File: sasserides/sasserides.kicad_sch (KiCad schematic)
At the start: 132 parts, among them J1 Conn_02x16_Odd_Even, Q1 2N7002, U1 CDCV304PW

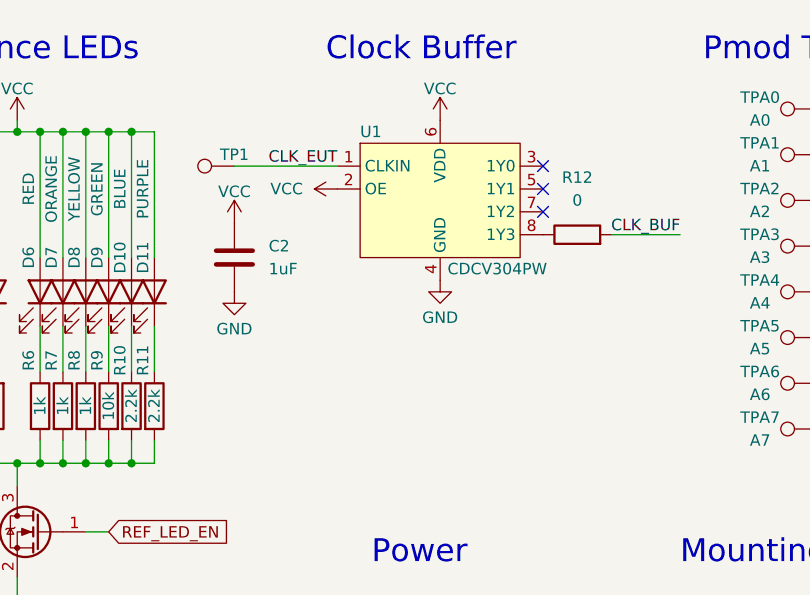
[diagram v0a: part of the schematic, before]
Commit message: Add a 1M pulldown resistor at clock buffer input.
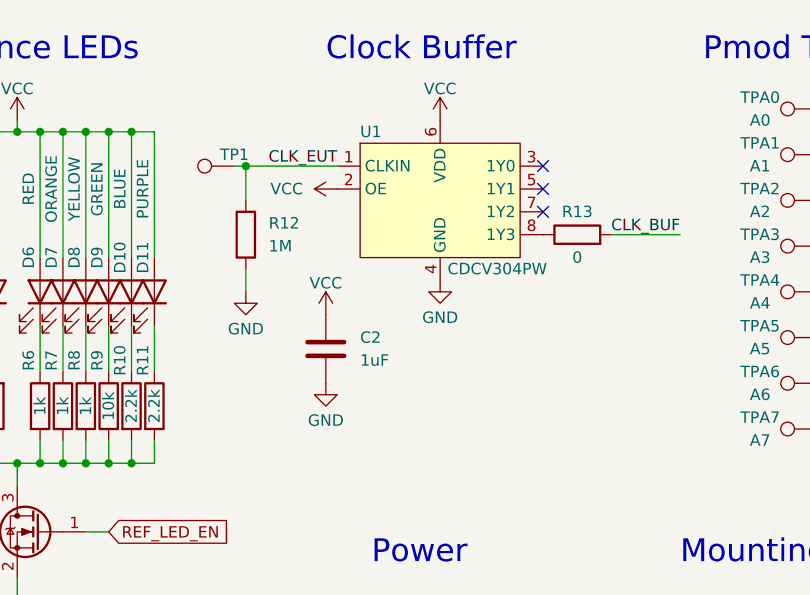
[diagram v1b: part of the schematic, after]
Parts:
- added R12: 1M, Resistor_SMD:R_0402_1005Metric, symbol Device:R
- renumbered R12 to R13
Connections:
- net CLK_EUT: now also R12.2
- net GND: now also R12.1
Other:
- moved on the sheet: C2
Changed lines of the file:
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@@
   (junction (at 33.02 114.3) (diameter 0) (color 0 0 0 0)
   )
+  (junction (at 60.96 118.11) (diameter 0) (color 0 0 0 0)
+  )
   (junction (at 45.72 114.3) (diameter 0) (color 0 0 0 0)
   )
@@
     (stroke (width 0) (type default))
   )
-  (wire (pts (xy 71.12 118.11) (xy 59.69 118.11))
+  (wire (pts (xy 71.12 118.11) (xy 60.96 118.11))
     (stroke (width 0) (type default))
   )
@@
     (stroke (width 0) (type default))
   )
+  (wire (pts (xy 60.96 118.11) (xy 60.96 121.92))
+    (stroke (width 0) (type default))
+  )
   (wire (pts (xy 85.09 74.93) (xy 106.68 74.93))
     (stroke (width 0) (type default))
@@
     (stroke (width 0) (type default))
   )
+  (wire (pts (xy 60.96 129.54) (xy 60.96 132.08))
+    (stroke (width 0) (type default))
+  )
   (wire (pts (xy 27.94 151.13) (xy 30.48 151.13))
     (stroke (width 0) (type default))
@@
     (stroke (width 0) (type default))
   )
+  (wire (pts (xy 60.96 118.11) (xy 59.69 118.11))
+    (stroke (width 0) (type default))
+  )
   (wire (pts (xy 25.4 128.27) (xy 25.4 114.3))
     (stroke (width 0) (type default))
@@
     )
   )
-  (symbol (lib_id "power:VCC") (at 59.69 124.46 0) (unit 1)
+  (symbol (lib_id "power:VCC") (at 69.85 134.62 0) (unit 1)
     (in_bom yes) (on_board yes) (dnp no)
-    (property "Reference" "#PWR011" (at 59.69 128.27 0)
+    (property "Reference" "#PWR011" (at 69.85 138.43 0)
       (effects (font (size 1.27 1.27)) hide)
     )
-    (property "Value" "VCC" (at 59.69 120.9581 0)
+    (property "Value" "VCC" (at 69.85 131.1181 0)
       (effects (font (size 1.27 1.27)))
     )
-    (property "Footprint" "" (at 59.69 124.46 0)
+    (property "Footprint" "" (at 69.85 134.62 0)
       (effects (font (size 1.27 1.27)) hide)
     )
-    (property "Datasheet" "" (at 59.69 124.46 0)
+    (property "Datasheet" "" (at 69.85 134.62 0)
       (effects (font (size 1.27 1.27)) hide)
     )
@@
     )
   )
-  (symbol (lib_id "Device:C") (at 59.69 128.27 0) (unit 1)
+  (symbol (lib_id "Device:C") (at 69.85 138.43 0) (unit 1)
     (in_bom yes) (on_board yes) (dnp no)
-    (property "Reference" "C2" (at 63.5 127 0)
+    (property "Reference" "C2" (at 73.66 137.16 0)
       (effects (font (size 1.27 1.27)) (justify left))
     )
-    (property "Value" "1uF" (at 63.5 129.54 0)
+    (property "Value" "1uF" (at 73.66 139.7 0)
       (effects (font (size 1.27 1.27)) (justify left))
     )
-    (property "Footprint" "Capacitor_SMD:C_0805_2012Metric" (at 60.6552 132.08 0)
+    (property "Footprint" "Capacitor_SMD:C_0805_2012Metric" (at 70.8152 142.24 0)
       (effects (font (size 1.27 1.27)) hide)
     )
-    (property "Datasheet" "~" (at 59.69 128.27 0)
+    (property "Datasheet" "~" (at 69.85 138.43 0)
       (effects (font (size 1.27 1.27)) hide)
     )
@@
     )
   )
-  (symbol (lib_id "power:GND") (at 59.69 132.08 0) (unit 1)
+  (symbol (lib_id "power:GND") (at 69.85 142.24 0) (unit 1)
     (in_bom yes) (on_board yes) (dnp no)
-    (property "Reference" "#PWR012" (at 59.69 138.43 0)
+    (property "Reference" "#PWR012" (at 69.85 148.59 0)
       (effects (font (size 1.27 1.27)) hide)
     )
-    (property "Value" "GND" (at 59.69 136.2155 0)
+    (property "Value" "GND" (at 69.85 146.3755 0)
       (effects (font (size 1.27 1.27)))
     )
-    (property "Footprint" "" (at 59.69 132.08 0)
+    (property "Footprint" "" (at 69.85 142.24 0)
       (effects (font (size 1.27 1.27)) hide)
     )
-    (property "Datasheet" "" (at 59.69 132.08 0)
+    (property "Datasheet" "" (at 69.85 142.24 0)
       (effects (font (size 1.27 1.27)) hide)
     )
@@
   )
   (symbol (lib_id "Device:R") (at 97.79 125.73 90) (unit 1)
-    (in_bom yes) (on_board yes) (dnp no) (fields_autoplaced)
-    (property "Reference" "R12" (at 97.79 119.38 90)
+    (in_bom yes) (on_board yes) (dnp no)
+    (property "Reference" "R13" (at 97.79 123.19 90)
       (effects (font (size 1.27 1.27)))
     )
-    (property "Value" "0" (at 97.79 121.92 90)
+    (property "Value" "0" (at 97.79 128.27 90)
       (effects (font (size 1.27 1.27)))
     )
@@
       (project "sasserides"
         (path "/29d14f83-224e-4982-8820-b9fb63f3a50c"
-          (reference "R12") (unit 1)
+          (reference "R13") (unit 1)
         )
       )
@@
     )
   )
+  (symbol (lib_id "power:GND") (at 60.96 132.08 0) (mirror y) (unit 1)
+    (in_bom yes) (on_board yes) (dnp no) (fields_autoplaced)
+    (property "Reference" "#PWR014" (at 60.96 138.43 0)
+      (effects (font (size 1.27 1.27)) hide)
+    )
+    (property "Value" "GND" (at 60.96 136.2155 0)
+      (effects (font (size 1.27 1.27)))
+    )
+    (property "Footprint" "" (at 60.96 132.08 0)
+      (effects (font (size 1.27 1.27)) hide)
+    )
+    (property "Datasheet" "" (at 60.96 132.08 0)
+      (effects (font (size 1.27 1.27)) hide)
+    )
+    (pin "1")
+    (instances
+      (project "sasserides"
+        (path "/29d14f83-224e-4982-8820-b9fb63f3a50c"
+          (reference "#PWR014") (unit 1)
+        )
+      )
+    )
+  )
   (symbol (lib_id "Device:C") (at 24.13 162.56 0) (mirror y) (unit 1)
     (in_bom yes) (on_board yes) (dnp no)
@@
         )
       )
+    )
+  )
+  (symbol (lib_id "Device:R") (at 60.96 125.73 180) (unit 1)
+    (in_bom yes) (on_board yes) (dnp no)
+    (property "Reference" "R12" (at 63.5 124.46 0)
+      (effects (font (size 1.27 1.27)) (justify right))
+    )
+    (property "Value" "1M" (at 63.5 127 0)
+      (effects (font (size 1.27 1.27)) (justify right))
+    )
+    (property "Footprint" "Resistor_SMD:R_0402_1005Metric" (at 62.738 125.73 90)
+      (effects (font (size 1.27 1.27)) hide)
+    )
+    (property "Datasheet" "~" (at 60.96 125.73 0)
+      (effects (font (size 1.27 1.27)) hide)
+    )
+    (pin "1")
+    (pin "2")
+    (instances
+      (project "sasserides"
+        (path "/29d14f83-224e-4982-8820-b9fb63f3a50c"
+          (reference "R12") (unit 1)
+        )
+      )

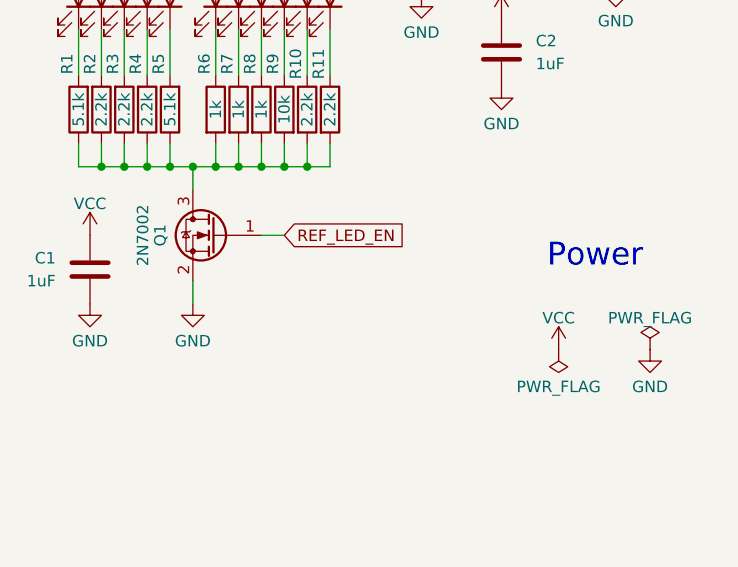
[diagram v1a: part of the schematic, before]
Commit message: Add 10k pulldown to Q1 gate.
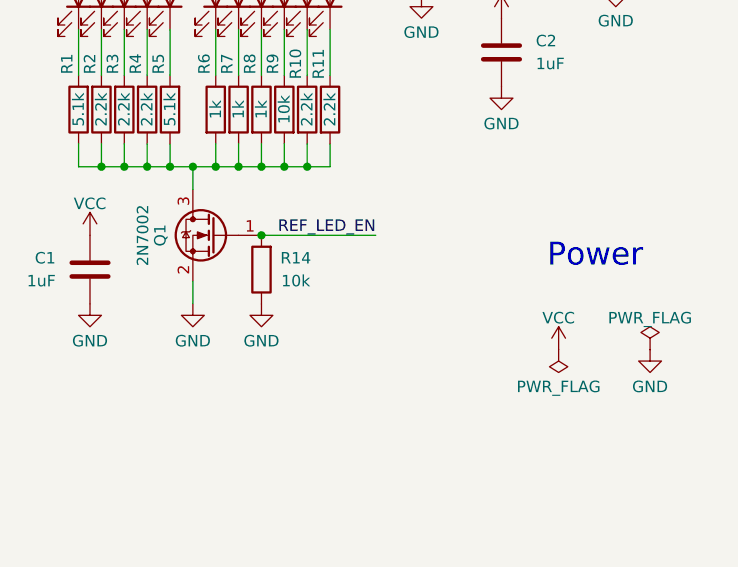
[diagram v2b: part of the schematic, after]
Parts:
- added R14: 10k, Resistor_SMD:R_0402_1005Metric, symbol Device:R
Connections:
- net GND: now also R14.1
- net REF_LED_EN: now also R14.2
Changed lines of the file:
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@@
   (junction (at 40.64 114.3) (diameter 0) (color 0 0 0 0)
   )
+  (junction (at 43.18 158.75) (diameter 0) (color 0 0 0 0)
+  )
   (junction (at 45.72 151.13) (diameter 0) (color 0 0 0 0)
   )
@@
     (stroke (width 0) (type default))
   )
-  (wire (pts (xy 45.72 158.75) (xy 43.18 158.75))
+  (wire (pts (xy 55.88 158.75) (xy 43.18 158.75))
     (stroke (width 0) (type default))
   )
@@
     (effects (font (size 2.54 2.54)) (justify left bottom))
   )
+  (label "REF_LED_EN" (at 55.88 158.75 180) (fields_autoplaced)
+    (effects (font (size 1.27 1.27)) (justify right bottom))
+  )
   (label "D2 3V3-Vf" (at 54.61 92.71 0) (fields_autoplaced)
     (effects (font (size 1.27 1.27)) (justify left bottom))
@@
     (effects (font (size 1.27 1.27)) (justify left bottom))
   )
-  (global_label "REF_LED_EN" (shape input) (at 45.72 158.75 0) (fields_autoplaced)
-    (effects (font (size 1.27 1.27)) (justify left))
-    (property "Intersheetrefs" "${INTERSHEET_REFS}" (at 59.9952 158.75 0)
-      (effects (font (size 1.27 1.27)) (justify left) hide)
-    )
-  )
   (symbol (lib_id "Connector:TestPoint") (at 203.2 59.69 90) (unit 1)
     (in_bom yes) (on_board yes) (dnp no)
@@
     )
   )
+  (symbol (lib_id "Device:R") (at 43.18 162.56 180) (unit 1)
+    (in_bom yes) (on_board yes) (dnp no)
+    (property "Reference" "R14" (at 46.99 161.29 0)
+      (effects (font (size 1.27 1.27)))
+    )
+    (property "Value" "10k" (at 46.99 163.83 0)
+      (effects (font (size 1.27 1.27)))
+    )
+    (property "Footprint" "Resistor_SMD:R_0402_1005Metric" (at 44.958 162.56 90)
+      (effects (font (size 1.27 1.27)) hide)
+    )
+    (property "Datasheet" "~" (at 43.18 162.56 0)
+      (effects (font (size 1.27 1.27)) hide)
+    )
+    (property "Part Number" "RC0402JR-0710KL" (at 43.18 162.56 0)
+      (effects (font (size 1.27 1.27)) hide)
+    )
+    (property "Substitution" "any equivalent" (at 43.18 162.56 0)
+      (effects (font (size 1.27 1.27)) hide)
+    )
+    (property "Description" "RES 10K OHM 5% 1/16W 0402" (at 43.18 162.56 0)
+      (effects (font (size 1.27 1.27)) hide)
+    )
+    (property "Manufacturer" "Yageo" (at 43.18 162.56 0)
+      (effects (font (size 1.27 1.27)) hide)
+    )
+    (pin "1")
+    (pin "2")
+    (instances
+      (project "sasserides"
+        (path "/29d14f83-224e-4982-8820-b9fb63f3a50c"
+          (reference "R14") (unit 1)
+        )
+      )
+      (project "tycho"
+        (path "/4ed1cbaf-15e8-40e5-8366-86487d525fd5"
+          (reference "R58") (unit 1)
+        )
+      )
+      (project "luna_rev0"
+        (path "/fb621148-8145-4217-9712-738e1b5a4823/00000000-0000-0000-0000-00005def5588"
+          (reference "R29") (unit 1)
+        )
+      )
+    )
+  )
   (symbol (lib_id "Connector:TestPoint") (at 129.54 111.76 270) (unit 1)
     (in_bom yes) (on_board yes) (dnp no) (fields_autoplaced)
@@
         )
       )
+    )
+  )
+  (symbol (lib_id "power:GND") (at 43.18 166.37 0) (unit 1)
+    (in_bom yes) (on_board yes) (dnp no) (fields_autoplaced)
+    (property "Reference" "#PWR015" (at 43.18 172.72 0)
+      (effects (font (size 1.27 1.27)) hide)
+    )
+    (property "Value" "GND" (at 43.18 170.5055 0)
+      (effects (font (size 1.27 1.27)))
+    )
+    (property "Footprint" "" (at 43.18 166.37 0)
+      (effects (font (size 1.27 1.27)) hide)
+    )
+    (property "Datasheet" "" (at 43.18 166.37 0)
+      (effects (font (size 1.27 1.27)) hide)
+    )
+    (pin "1")
+    (instances
+      (project "sasserides"
+        (path "/29d14f83-224e-4982-8820-b9fb63f3a50c"
+          (reference "#PWR015") (unit 1)
+        )
+      )

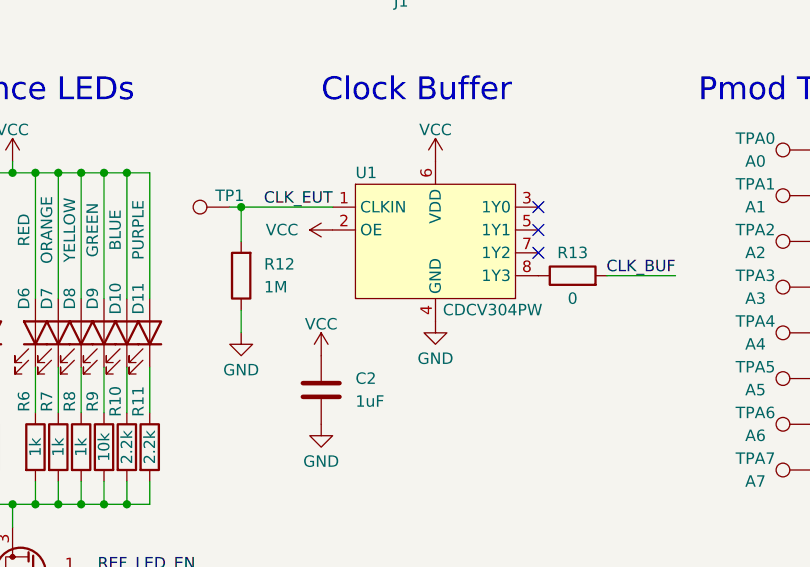
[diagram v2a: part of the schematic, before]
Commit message: Add part numbers; Change C1 & C2 to 0603 parts
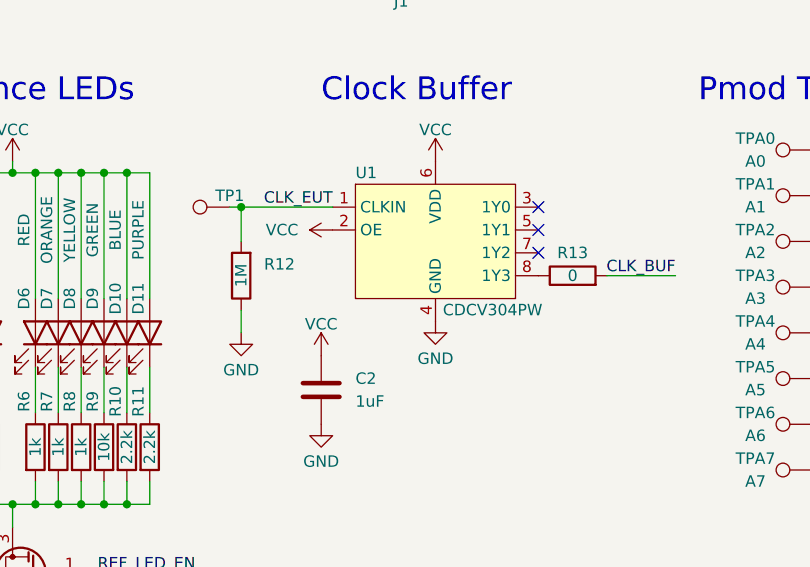
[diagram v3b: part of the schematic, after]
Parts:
- C1, C2: footprint Capacitor_SMD:C_0805_2012Metric -> Capacitor_SMD:C_0603_1608Metric_Pad1.08x0.95mm_HandSolder; Manufacturer (none) -> Murata Electronics; Part Number (none) -> GRT188R61H105ME13D; Substitution (none) -> any equivalent
- R12: Manufacturer (none) -> VO; Part Number (none) -> SCR0402F1M
- R13: Manufacturer (none) -> Vishay Dale; Part Number (none) -> CRCW04020000Z0ED
- U1: Manufacturer (none) -> Texas Instruments; Part Number (none) -> CDCV304PWR
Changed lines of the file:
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@@
       (effects (font (size 1.27 1.27)) (justify left))
     )
-    (property "Footprint" "Capacitor_SMD:C_0805_2012Metric" (at 70.8152 142.24 0)
+    (property "Footprint" "Capacitor_SMD:C_0603_1608Metric_Pad1.08x0.95mm_HandSolder" (at 70.8152 142.24 0)
       (effects (font (size 1.27 1.27)) hide)
     )
@@
       (effects (font (size 1.27 1.27)) hide)
     )
+    (property "Manufacturer" "Murata Electronics" (at 69.85 138.43 0)
+      (effects (font (size 1.27 1.27)) hide)
+    )
+    (property "Part Number" "GRT188R61H105ME13D" (at 69.85 138.43 0)
+      (effects (font (size 1.27 1.27)) hide)
+    )
+    (property "Description" "CAP CER 1UF 50V X5R 0603" (at 69.85 138.43 0)
+      (effects (font (size 1.27 1.27)) hide)
+    )
+    (property "Substitution" "any equivalent" (at 69.85 138.43 0)
+      (effects (font (size 1.27 1.27)) hide)
+    )
     (pin "1")
     (pin "2")
@@
       (effects (font (size 1.27 1.27)) hide)
     )
+    (property "Manufacturer" "Texas Instruments" (at 82.55 121.92 0)
+      (effects (font (size 1.27 1.27)) hide)
+    )
+    (property "Part Number" "CDCV304PWR" (at 82.55 121.92 0)
+      (effects (font (size 1.27 1.27)) hide)
+    )
+    (property "Description" "2.3V~3.6V 200MHz TSSOP-8  Clock Buffers, Drivers ROHS" (at 82.55 121.92 0)
+      (effects (font (size 1.27 1.27)) hide)
+    )
     (pin "1")
     (pin "2")
@@
       (effects (font (size 1.27 1.27)))
     )
-    (property "Value" "0" (at 97.79 128.27 90)
+    (property "Value" "0" (at 97.79 125.73 90)
       (effects (font (size 1.27 1.27)))
     )
@@
       (effects (font (size 1.27 1.27)) hide)
     )
+    (property "Manufacturer" "Vishay Dale" (at 97.79 125.73 0)
+      (effects (font (size 1.27 1.27)) hide)
+    )
+    (property "Part Number" "CRCW04020000Z0ED" (at 97.79 125.73 0)
+      (effects (font (size 1.27 1.27)) hide)
+    )
+    (property "Description" "RES SMD 0 OHM JUMPER 1/16W 0402" (at 97.79 125.73 0)
+      (effects (font (size 1.27 1.27)) hide)
+    )
     (pin "1")
     (pin "2")
@@
       (effects (font (size 1.27 1.27)) (justify left))
     )
-    (property "Footprint" "Capacitor_SMD:C_0805_2012Metric" (at 23.1648 166.37 0)
+    (property "Footprint" "Capacitor_SMD:C_0603_1608Metric_Pad1.08x0.95mm_HandSolder" (at 23.1648 166.37 0)
       (effects (font (size 1.27 1.27)) hide)
     )
@@
       (effects (font (size 1.27 1.27)) hide)
     )
+    (property "Manufacturer" "Murata Electronics" (at 24.13 162.56 0)
+      (effects (font (size 1.27 1.27)) hide)
+    )
+    (property "Part Number" "GRT188R61H105ME13D" (at 24.13 162.56 0)
+      (effects (font (size 1.27 1.27)) hide)
+    )
+    (property "Description" "CAP CER 1UF 50V X5R 0603" (at 24.13 162.56 0)
+      (effects (font (size 1.27 1.27)) hide)
+    )
+    (property "Substitution" "any equivalent" (at 24.13 162.56 0)
+      (effects (font (size 1.27 1.27)) hide)
+    )
     (pin "1")
     (pin "2")
@@
       (effects (font (size 1.27 1.27)) (justify right))
     )
-    (property "Value" "1M" (at 63.5 127 0)
+    (property "Value" "1M" (at 60.96 127 90)
       (effects (font (size 1.27 1.27)) (justify right))
     )
@@
       (effects (font (size 1.27 1.27)) hide)
     )
+    (property "Manufacturer" "VO" (at 60.96 125.73 0)
+      (effects (font (size 1.27 1.27)) hide)
+    )
+    (property "Part Number" "SCR0402F1M" (at 60.96 125.73 0)
+      (effects (font (size 1.27 1.27)) hide)
+    )
+    (property "Description" "±1% 1MΩ 0402 Chip Resistor - Surface Mount ROHS Copy" (at 60.96 125.73 0)
+      (effects (font (size 1.27 1.27)) hide)
+    )
